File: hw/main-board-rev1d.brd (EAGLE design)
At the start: 100 x 88 mm, 34 parts, among them U2 MIC5504, X1 3v7 lipo, X2 ESP-12, X3 MOD-TP4056

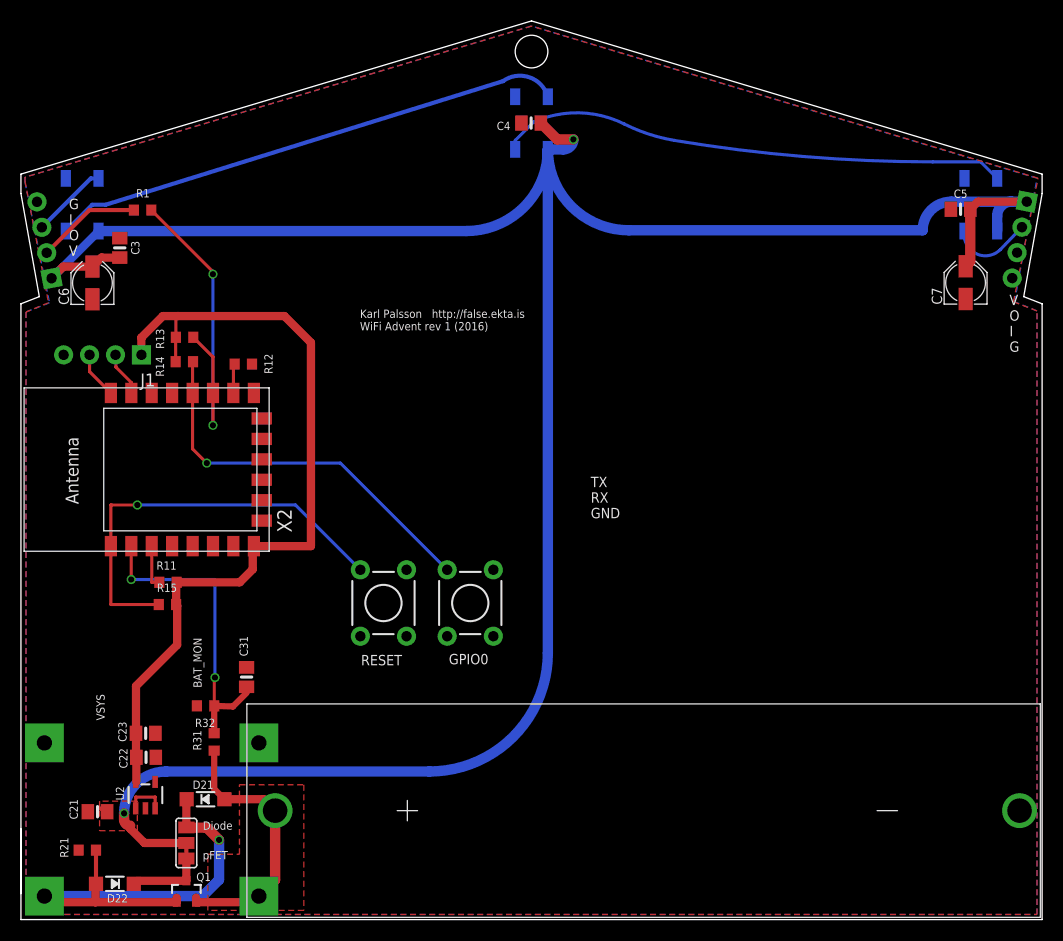
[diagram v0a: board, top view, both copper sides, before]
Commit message: hw rev 1.2
Moved module to side for "proper" rf.
Fixed rotated wing connectors
Fixed overlapping polygon pours
Relaid out almost all of the lower section
Added more test points, and all spare ios on ESPmodule
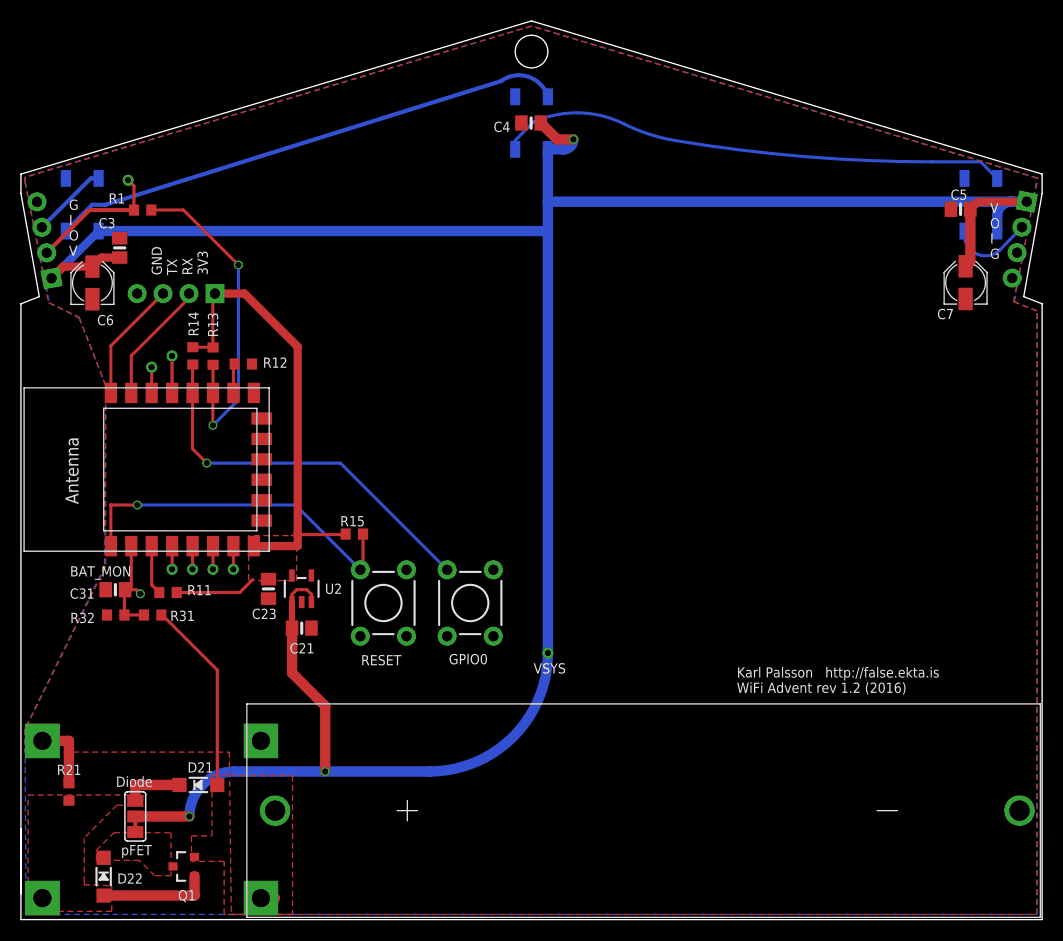
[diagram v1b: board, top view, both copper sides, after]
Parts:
- removed C22: 10uF, microbuilder:0805-NO
- added TP1, TP2, TP3, TP4, TP5, TP6, TP7, TP8: (no value), karls-parts-2016-09:TP_06TH
- moved C21 26.9 mm to (27.5, 28.5), turned to 0 degrees
- moved U2 25.3 mm to (27.5, 32.4)
- moved R15 19.6 mm to (32.7, 37.7), turned to 180 degrees
- moved C23 18.6 mm to (24.2, 32.4), turned to 270 degrees
- moved C31 15.4 mm to (9.25, 32.3), turned to 180 degrees
- moved R31 13.8 mm to (12.9, 29.8), turned to 0 degrees
- moved R32 12.5 mm to (9.28, 29.8)
- moved J1 9.37 mm to (19.0, 61.3)
- moved R21 5.98 mm to (4.70, 12.5), turned to 90 degrees
- moved JP2 5.64 mm to (11.2, 10.1)
- moved R13 3.35 mm to (18.8, 55.2), turned to 90 degrees
- moved Q1 2.51 mm to (16.0, 5.20), turned to 90 degrees
- moved D21 1.57 mm to (17.4, 13.2)
- moved D22 1.30 mm to (8.10, 4.20), turned to 270 degrees
- moved R14 1.00 mm to (16.8, 55.2), turned to 90 degrees
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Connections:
- new net N$1: TP1.P$1, X2.4
- new net N$2: TP2.P$1, X2.5
- new net N$4: TP3.P$1, X2.6
- new net N$5: TP4.P$1, X2.7
- new net N$6: TP5.P$1, X2.14
- new net N$7: TP6.P$1, X2.13
- net 3.3V: no longer C22.1
- net GND: no longer C22.2
- net LEFT_IN: now also TP8.P$1
- net VSYS: now also TP7.P$1
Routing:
- net VBUS: track 46.9 -> 16.7 mm, vias 1 -> 0
- net 3.3V: track 82.0 -> 54.3 mm
- net BAT_MON: track 30.9 -> 10.4 mm, vias 2 -> 1
- net RXD: track 4.37 -> 12.1 mm
- net N$3: track 7.45 -> 0.00 mm
- net TXD: track 4.60 -> 11.8 mm
- net RESET: track 42.1 -> 35.3 mm
- net GND: track 0.00 -> 6.75 mm
- net VBAT: track 26.5 -> 20.4 mm
- net N$7: track 0.00 -> 3.63 mm
- net LEFT_IN: track 10.3 -> 13.4 mm
- net N$6: track 0.00 -> 2.53 mm
- net N$5: track 0.00 -> 2.27 mm
- net N$4: track 0.00 -> 2.27 mm
- net N$2: track 0.00 -> 2.27 mm
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- added copper zone on layer 1, net 3.3V
- added copper zone on layer 1, net N$3
- added copper zone on layer 1, net VBUS
- removed copper zone on layer 1, net VSYS
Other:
- board text added: "GND TX RX 3V3"
- board text added: "Karl Palsson http://false.ekta.is WiFi Advent rev 1.2 (2016)"
- board text removed: "Karl Palsson http://false.ekta.is WiFi Advent rev 1 (2016)"
- board text removed: "TX RX GND"
